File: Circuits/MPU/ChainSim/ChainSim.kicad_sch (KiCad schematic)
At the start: 12 parts, among them U1 ADA4805-2ARMZ, U2 LT1715

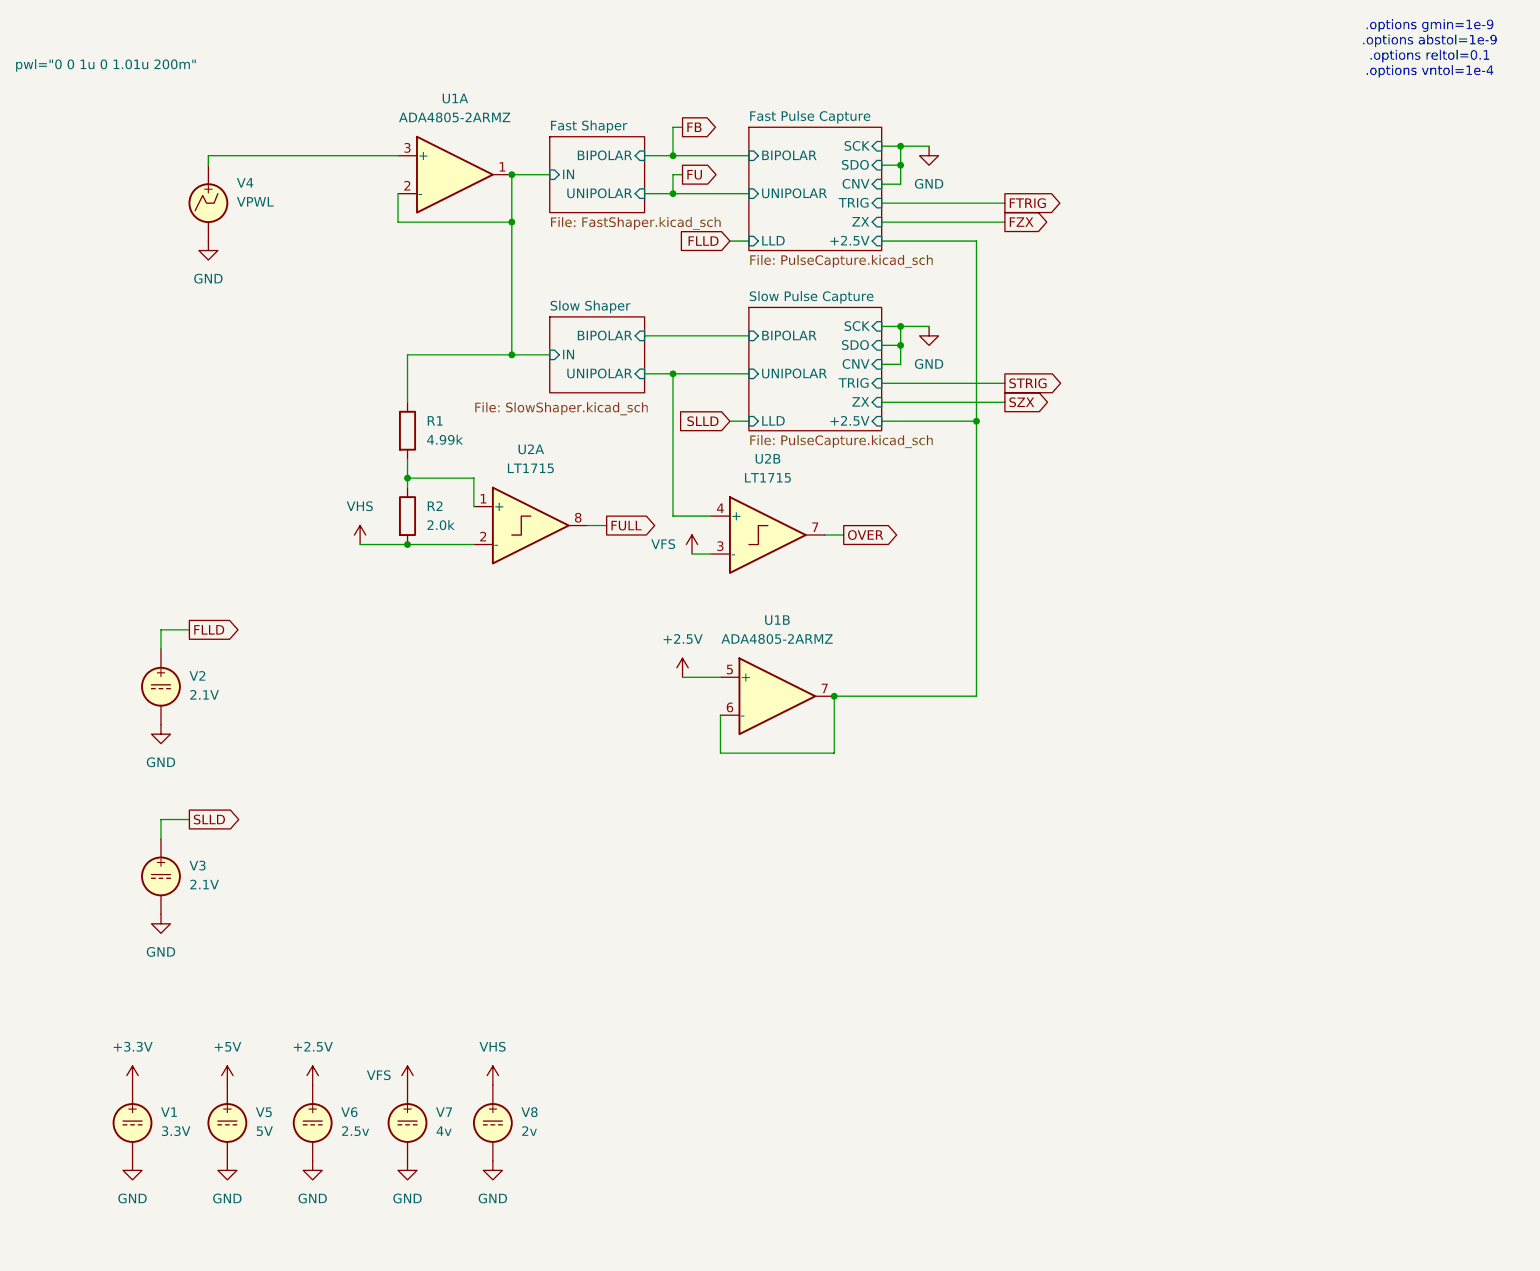
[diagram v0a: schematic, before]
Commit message: Chainsim working, a little tuneup
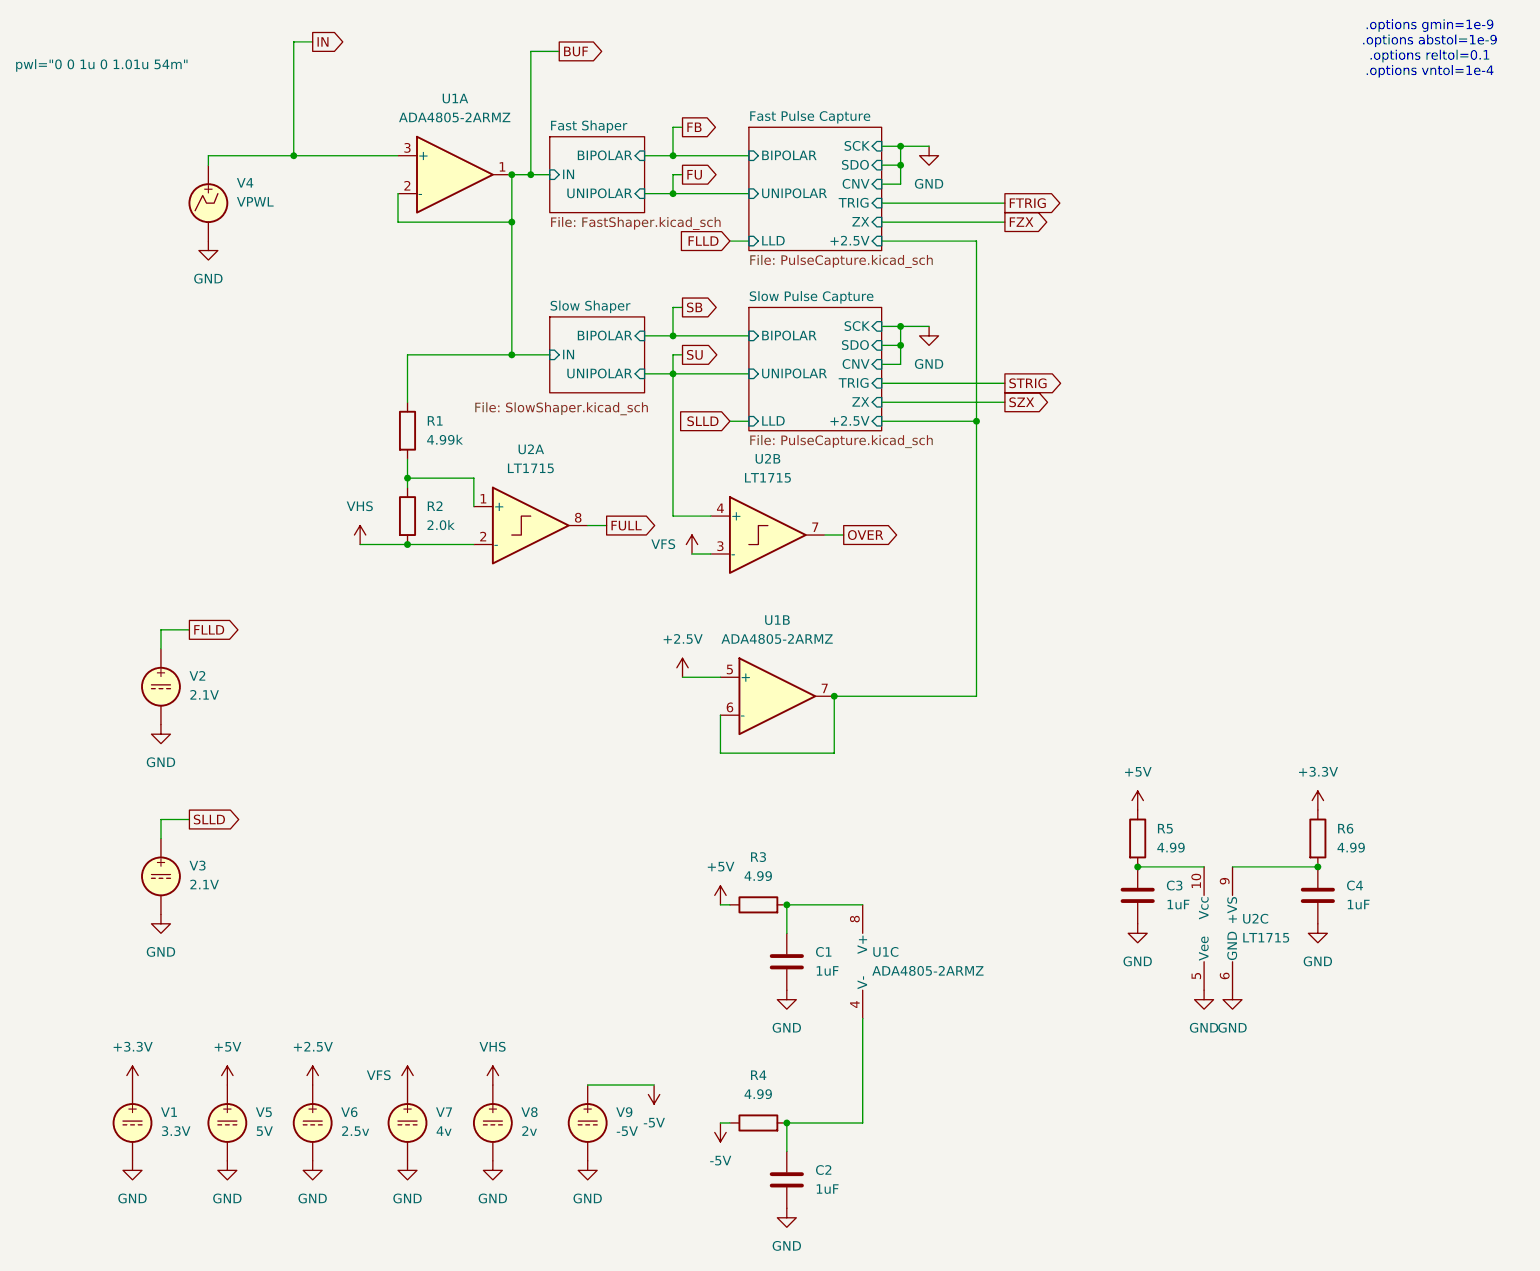
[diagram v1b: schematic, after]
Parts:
- added C1, C2, C3, C4: 1uF, Capacitor_SMD:C_0805_2012Metric, symbol QuERI_symbols:C
- added R3, R4, R5, R6: 4.99, Resistor_SMD:R_0603_1608Metric, symbol QuERI_symbols:Rlowp
- added unit 3 of U1
- added unit 3 of U2
- added V9: -5V, symbol Simulation_SPICE:VDC
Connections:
- net +3.3V: now also R6.1
- net +5V: now also R3.1, R5.1
- net GND: now also C1.2, C2.2, C3.2, C4.2, U2.5 (Vee), U2.6 (GND), V9.2
- net IN: now reaches U1.3 (+), V4.1
- net Fast Shaper/IN renamed BUF
- net Slow Pulse Capture/UNIPOLAR renamed SU
- new net: C4.1, R6.2, U2.9 (+VS)
- new net: C1.1, R3.2, U1.8 (V+)
- new net: C2.1, R4.2, U1.4 (V-)
- new net: C3.1, R5.2, U2.10 (Vcc)
- new net -5V: R4.1, V9.1
